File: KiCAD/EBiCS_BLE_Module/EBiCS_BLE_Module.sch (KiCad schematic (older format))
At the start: 9 parts

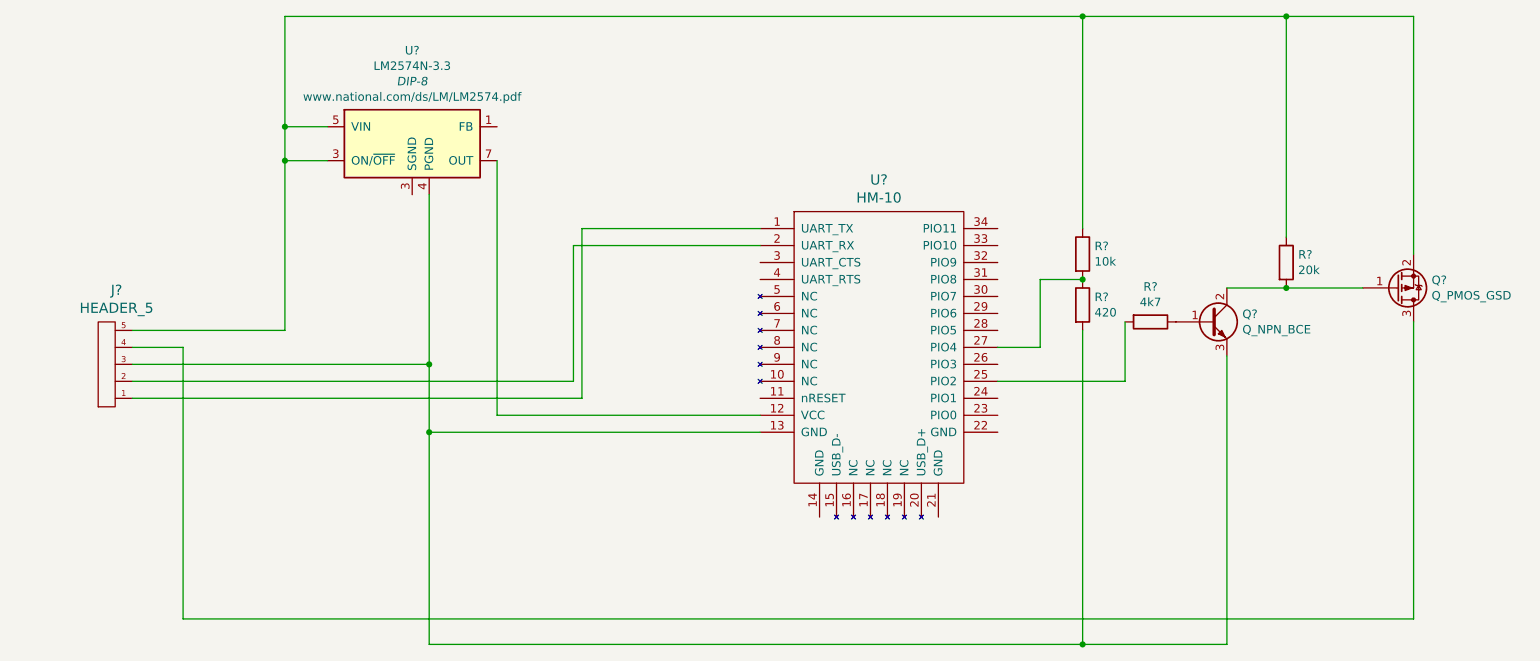
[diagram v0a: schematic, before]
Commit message: switched back to the old KM5S processing.
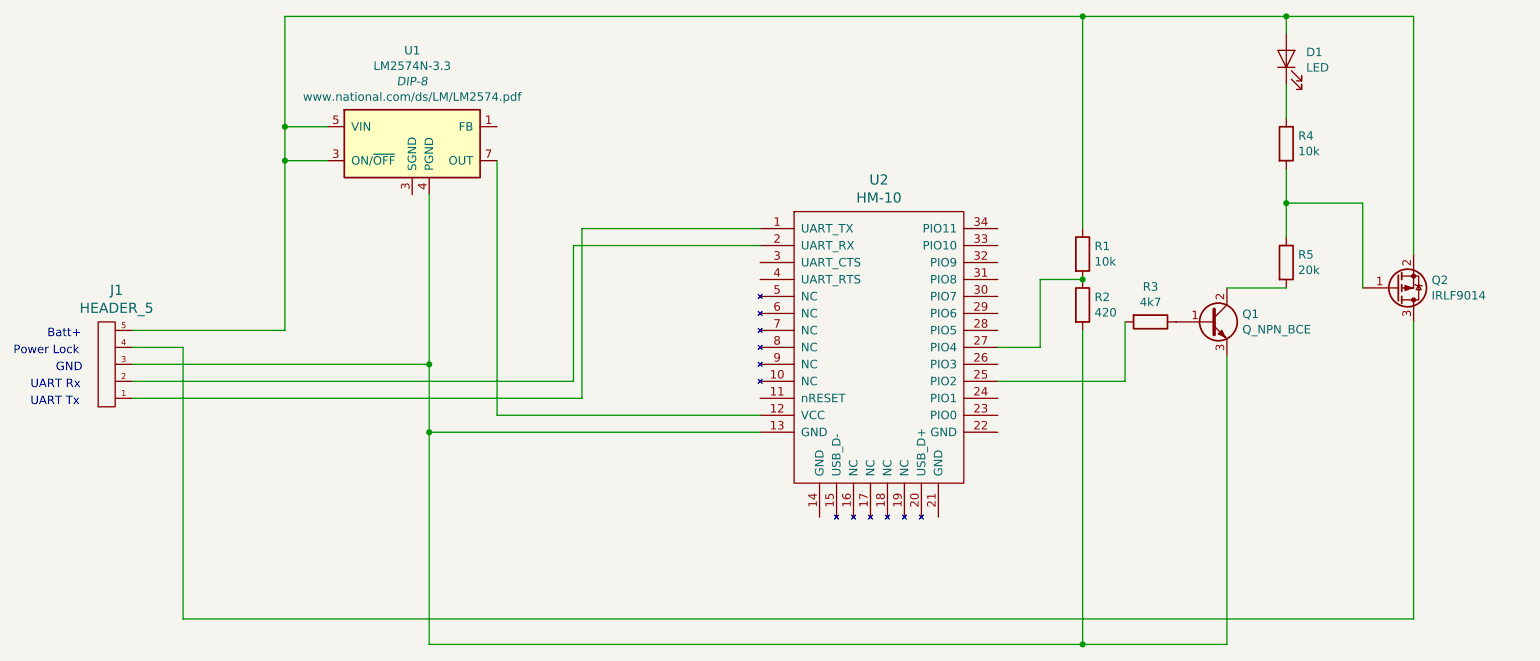
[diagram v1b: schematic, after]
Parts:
- added D1: LED, symbol Device:LED
- added R4: 10k, symbol Device:R
- Q2: renamed from Q?; value Q_PMOS_GSD -> IRLF9014
- gave numbers to parts that had none: 8
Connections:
- net at U1.3 (SGND): now also J1.5, Q2.2 (S), R1.1, U1.5 (VIN), D1.2 (A)
- net at Q1.2 (C), R5.2: no longer Q2.1 (G)
- new net: Q2.1 (G), R4.2, R5.1
- new net: D1.1 (K), R4.1
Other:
- note added: "Batt+"
- note added: "GND"
- note added: "Power Lock"
- note added: "UART Rx"
- note added: "UART Tx"
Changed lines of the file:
@@
 EESchema Schematic File Version 4
+LIBS:EBiCS_BLE_Module-cache
 EELAYER 30 0
 EELAYER END
@@
 $EndDescr
 $Comp
-L HM-10:HM-10 U?
+L HM-10:HM-10 U2
 U 1 1 5FA814D7
 P 6100 3800
-F 0 "U?" H 6050 4837 60  0000 C CNN
+F 0 "U2" H 6050 4837 60  0000 C CNN
 F 1 "HM-10" H 6050 4731 60  0000 C CNN
 F 2 "" H 5850 4550 60  0001 C CNN
@@
 $EndComp
 $Comp
-L DC-DC:LM2574N-3.3 U?
+L DC-DC:LM2574N-3.3 U1
 U 1 1 5FA8238A
 P 3300 2550
-F 0 "U?" H 3300 3099 50  0000 C CNN
+F 0 "U1" H 3300 3099 50  0000 C CNN
 F 1 "LM2574N-3.3" H 3300 3008 50  0000 C CNN
 F 2 "DIP-8" H 3300 2917 50  0000 C CIN
@@
 $EndComp
 $Comp
-L JST:HEADER_5 J?
+L JST:HEADER_5 J1
 U 1 1 5FA837D2
 P 1550 3850
-F 0 "J?" H 1542 3413 60  0000 C CNN
+F 0 "J1" H 1542 3413 60  0000 C CNN
 F 1 "HEADER_5" H 1542 3519 60  0000 C CNN
 F 2 "" H 1550 3850 60  0000 C CNN
@@
 	3800 4150 5350 4150
 $Comp
-L Device:Q_PMOS_GSD Q?
+L Device:Q_PMOS_GSD Q2
 U 1 1 5FA88256
 P 9100 3400
-F 0 "Q?" H 9306 3354 50  0000 L CNN
-F 1 "Q_PMOS_GSD" H 9306 3445 50  0000 L CNN
+F 0 "Q2" H 9306 3354 50  0000 L CNN
+F 1 "IRLF9014" H 9306 3445 50  0000 L CNN
 F 2 "" H 9300 3500 50  0001 C CNN
 F 3 "~" H 9100 3400 50  0001 C CNN
@@
 $EndComp
 $Comp
-L Device:Q_NPN_BCE Q?
+L Device:Q_NPN_BCE Q1
 U 1 1 5FA88D7B
 P 8000 3600
-F 0 "Q?" H 8191 3646 50  0000 L CNN
+F 0 "Q1" H 8191 3646 50  0000 L CNN
 F 1 "Q_NPN_BCE" H 8191 3555 50  0000 L CNN
 F 2 "" H 8200 3700 50  0001 C CNN
@@
 $EndComp
 $Comp
-L Device:R R?
+L Device:R R5
 U 1 1 5FA8B0CA
 P 8450 3250
-F 0 "R?" H 8520 3296 50  0000 L CNN
+F 0 "R5" H 8520 3296 50  0000 L CNN
 F 1 "20k" H 8520 3205 50  0000 L CNN
 F 2 "" V 8380 3250 50  0001 C CNN
@@
 	8100 3400 8450 3400
 $Comp
-L Device:R R?
+L Device:R R3
 U 1 1 5FA8D17F
 P 7650 3600
-F 0 "R?" V 7443 3600 50  0000 C CNN
+F 0 "R3" V 7443 3600 50  0000 C CNN
 F 1 "4k7" V 7534 3600 50  0000 C CNN
 F 2 "" V 7580 3600 50  0001 C CNN
@@
 	1950 3750 1650 3750
 $Comp
-L Device:R R?
+L Device:R R1
 U 1 1 5FA8FDE2
 P 7250 3200
-F 0 "R?" H 7320 3246 50  0000 L CNN
+F 0 "R1" H 7320 3246 50  0000 L CNN
 F 1 "10k" H 7320 3155 50  0000 L CNN
 F 2 "" V 7180 3200 50  0001 C CNN
@@
 $EndComp
 $Comp
-L Device:R R?
+L Device:R R2
 U 1 1 5FA9045D
 P 7250 3500
-F 0 "R?" H 7320 3546 50  0000 L CNN
+F 0 "R2" H 7320 3546 50  0000 L CNN
 F 1 "420" H 7320 3455 50  0000 L CNN
 F 2 "" V 7180 3500 50  0001 C CNN
@@
 	7000 3750 6750 3750
 Connection ~ 7250 3350
-Connection ~ 8450 3400
-Wire Wire Line
-	8450 3400 8900 3400
+$Comp
+L Device:LED D1
+U 1 1 5FAC254D
+P 8450 2050
+F 0 "D1" V 8489 1933 50  0000 R CNN
+F 1 "LED" V 8398 1933 50  0000 R CNN
+F 2 "" H 8450 2050 50  0001 C CNN
+F 3 "~" H 8450 2050 50  0001 C CNN
+	1    8450 2050
+	0    -1   -1   0
+$EndComp
+$Comp
+L Device:R R4
+U 1 1 5FAC4085
+P 8450 2550
+F 0 "R4" H 8520 2596 50  0000 L CNN
+F 1 "10k" H 8520 2505 50  0000 L CNN
+F 2 "" V 8380 2550 50  0001 C CNN
+F 3 "~" H 8450 2550 50  0001 C CNN
+	1    8450 2550
+	1    0    0    -1
+$EndComp
 Wire Wire Line
 	7250 1800 8450 1800
 Wire Wire Line
-	8450 3100 8450 1800
+	8450 1800 8450 1900
 Connection ~ 8450 1800
 Wire Wire Line
 	8450 1800 9200 1800
+Wire Wire Line
+	8450 2200 8450 2400
+Wire Wire Line
+	8450 2700 8450 2900
+Wire Wire Line
+	8450 2900 8900 2900
+Wire Wire Line
+	8900 2900 8900 3400
+Connection ~ 8450 2900
+Wire Wire Line
+	8450 2900 8450 3100
+Text Notes 1150 3700 0    50   ~ 0
+Batt+
+Text Notes 950  3800 0    50   ~ 0
+Power Lock
+Text Notes 1200 3900 0    50   ~ 0
+GND
+Text Notes 1050 4000 0    50   ~ 0
+UART Rx
+Text Notes 1050 4100 0    50   ~ 0
+UART Tx
 $EndSCHEMATC
